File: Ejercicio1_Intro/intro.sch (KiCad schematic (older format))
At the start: 5 parts, among them K1 CONN_3

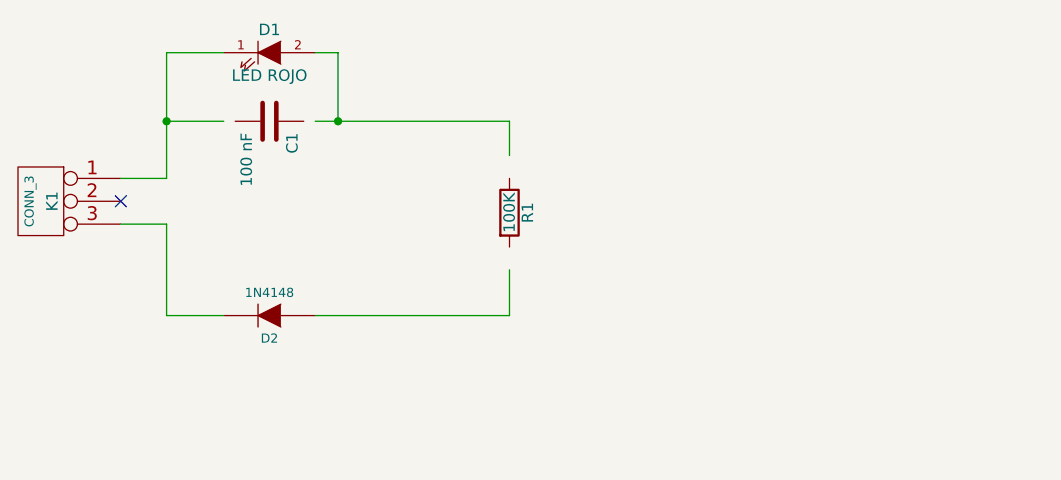
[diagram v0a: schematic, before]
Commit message: Agregado de asociación de footprints en el esquemático.
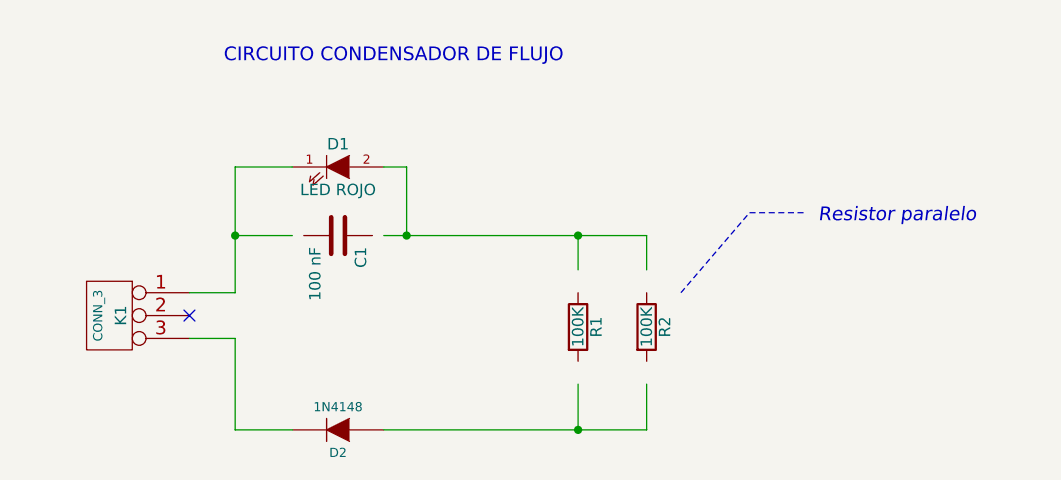
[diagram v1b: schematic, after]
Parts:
- added R2: 100K, footprints_ej1:R3-LARGE_PADS, symbol R
- C1: footprint (none) -> footprints_ej1:C_Rect_L7_W3.5_P5
- D1: footprint (none) -> footprints_ej1:LED-3MM
- D2: footprint (none) -> footprints_ej1:Diode_DO-35_SOD27_Horizontal_RM10
- K1: footprint (none) -> footprints_ej1:bornier3
- R1: footprint (none) -> footprints_ej1:R3-LARGE_PADS
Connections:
- wire segments 13 -> 15
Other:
- note added: "CIRCUITO CONDENSADOR DE FLUJO"
- note added: "Resistor paralelo"
- moved on the sheet: C1, D1, D2, K1, R1
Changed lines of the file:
@@
 LIBS:contrib
 LIBS:valves
+LIBS:intro-cache
 EELAYER 25 0
 EELAYER END
@@
 L C C1
 U 1 1 5638F4A6
-P 5050 3350
-F 0 "C1" H 5100 3450 50  0000 L CNN
-F 1 "100 nF" H 5100 3250 50  0000 L CNN
-F 2 "" H 5050 3350 60  0000 C CNN
-F 3 "" H 5050 3350 60  0000 C CNN
-	1    5050 3350
+P 5350 3850
+F 0 "C1" H 5400 3950 50  0000 L CNN
+F 1 "100 nF" H 5400 3750 50  0000 L CNN
+F 2 "footprints_ej1:C_Rect_L7_W3.5_P5" H 5350 3850 60  0001 C CNN
+F 3 "" H 5350 3850 60  0000 C CNN
+	1    5350 3850
 	0    1    1    0
 $EndComp
@@
 L R R1
 U 1 1 5638F4E1
-P 6100 3750
-F 0 "R1" V 6180 3750 50  0000 C CNN
-F 1 "100K" V 6100 3750 50  0000 C CNN
-F 2 "" H 6100 3750 60  0000 C CNN
-F 3 "" H 6100 3750 60  0000 C CNN
-	1    6100 3750
+P 6400 4250
+F 0 "R1" V 6480 4250 50  0000 C CNN
+F 1 "100K" V 6400 4250 50  0000 C CNN
+F 2 "footprints_ej1:R3-LARGE_PADS" H 6400 4250 60  0001 C CNN
+F 3 "" H 6400 4250 60  0000 C CNN
+	1    6400 4250
 	1    0    0    -1
 $EndComp
@@
 L DIODE D2
 U 1 1 5638F55C
-P 5050 4200
-F 0 "D2" H 5050 4300 40  0000 C CNN
-F 1 "1N4148" H 5050 4100 40  0000 C CNN
-F 2 "" H 5050 4200 60  0000 C CNN
-F 3 "" H 5050 4200 60  0000 C CNN
-	1    5050 4200
+P 5350 4700
+F 0 "D2" H 5350 4800 40  0000 C CNN
+F 1 "1N4148" H 5350 4600 40  0000 C CNN
+F 2 "footprints_ej1:Diode_DO-35_SOD27_Horizontal_RM10" H 5350 4700 60  0001 C CNN
+F 3 "" H 5350 4700 60  0000 C CNN
+	1    5350 4700
 	-1   0    0    1
 $EndComp
 Wire Wire Line
-	4600 3600 4400 3600
+	4900 4100 4700 4100
 Wire Wire Line
-	4600 3050 4600 3600
+	4900 3550 4900 4100
 Wire Wire Line
-	4600 3350 4850 3350
+	4900 3850 5150 3850
 Wire Wire Line
-	5250 3350 6100 3350
+	5550 3850 6700 3850
 Wire Wire Line
-	6100 3350 6100 3500
+	6400 3850 6400 4000
 Wire Wire Line
-	6100 4000 6100 4200
+	6400 4500 6400 4700
 Wire Wire Line
-	6100 4200 5250 4200
+	5550 4700 6700 4700
 Wire Wire Line
-	4850 4200 4600 4200
+	5150 4700 4900 4700
 Wire Wire Line
-	4600 4200 4600 3800
+	4900 4700 4900 4300
 Wire Wire Line
-	4600 3800 4400 3800
+	4900 4300 4700 4300
 $Comp
 L LED D1
 U 1 1 5638F7A0
-P 5050 3050
-F 0 "D1" H 5050 3150 50  0000 C CNN
-F 1 "LED ROJO" H 5050 2950 50  0000 C CNN
-F 2 "" H 5050 3050 60  0000 C CNN
-F 3 "" H 5050 3050 60  0000 C CNN
-	1    5050 3050
+P 5350 3550
+F 0 "D1" H 5350 3650 50  0000 C CNN
+F 1 "LED ROJO" H 5350 3450 50  0000 C CNN
+F 2 "footprints_ej1:LED-3MM" H 5350 3550 60  0001 C CNN
+F 3 "" H 5350 3550 60  0000 C CNN
+	1    5350 3550
 	1    0    0    -1
 $EndComp
 Wire Wire Line
-	5250 3050 5350 3050
+	5550 3550 5650 3550
 Wire Wire Line
-	5350 3050 5350 3350
-Connection ~ 5350 3350
+	5650 3550 5650 3850
+Connection ~ 5650 3850
 Wire Wire Line
-	4850 3050 4600 3050
-Connection ~ 4600 3350
+	5150 3550 4900 3550
+Connection ~ 4900 3850
 $Comp
 L CONN_3 K1
 U 1 1 5638F7EF
-P 4050 3700
-F 0 "K1" V 4000 3700 50  0000 C CNN
-F 1 "CONN_3" V 4100 3700 40  0000 C CNN
-F 2 "" H 4050 3700 60  0000 C CNN
-F 3 "" H 4050 3700 60  0000 C CNN
-	1    4050 3700
+P 4350 4200
+F 0 "K1" V 4300 4200 50  0000 C CNN
+F 1 "CONN_3" V 4400 4200 40  0000 C CNN
+F 2 "footprints_ej1:bornier3" H 4350 4200 60  0001 C CNN
+F 3 "" H 4350 4200 60  0000 C CNN
+	1    4350 4200
 	-1   0    0    -1
 $EndComp
-NoConn ~ 4400 3700
+NoConn ~ 4700 4200
+$Comp
+L R R2
+U 1 1 56390399
+P 6700 4250
+F 0 "R2" V 6780 4250 50  0000 C CNN
+F 1 "100K" V 6700 4250 50  0000 C CNN
+F 2 "footprints_ej1:R3-LARGE_PADS" H 7500 4500 60  0001 C CNN
+F 3 "" H 6700 4250 60  0000 C CNN
+	1    6700 4250
+	1    0    0    -1
+$EndComp
+Wire Wire Line
+	6700 3850 6700 4000
+Connection ~ 6400 3850
+Wire Wire Line
+	6700 4700 6700 4500
+Connection ~ 6400 4700
+Text Notes 4850 3100 0    60   ~ 0
+CIRCUITO CONDENSADOR DE FLUJO
+Wire Notes Line
+	6850 4100 7150 3750
+Wire Notes Line
+	7150 3750 7400 3750
+Text Notes 7450 3800 0    60   Italic 0
+Resistor paralelo
 $EndSCHEMATC

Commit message: Emprolijo esquemático.
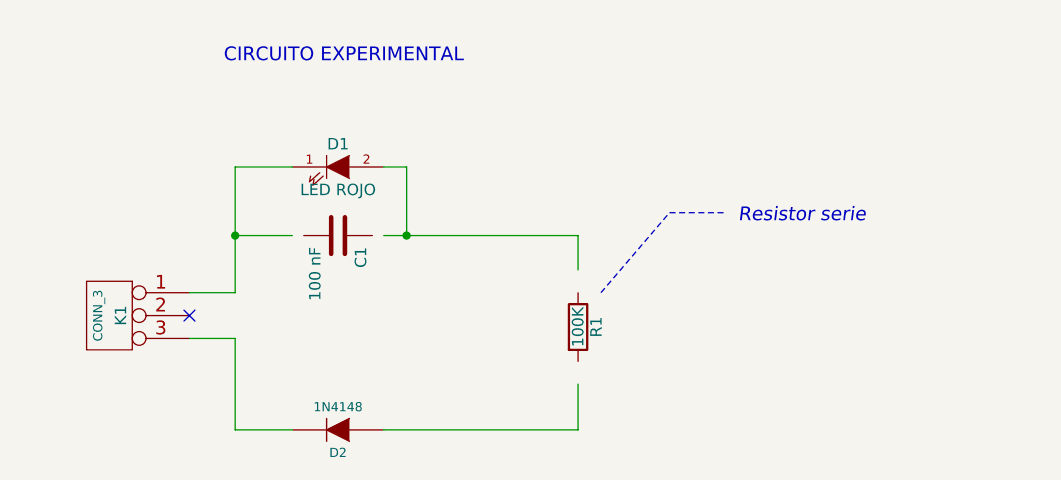
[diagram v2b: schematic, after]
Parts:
- removed R2: 100K, footprints_ej1:R3-LARGE_PADS, symbol R
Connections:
- wire segments 15 -> 13
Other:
- note added: "CIRCUITO EXPERIMENTAL"
- note added: "Resistor serie"
- note removed: "CIRCUITO CONDENSADOR DE FLUJO"
- note removed: "Resistor paralelo"
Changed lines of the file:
@@
 	4900 3850 5150 3850
-Wire Wire Line
-	5550 3850 6700 3850
 Wire Wire Line
 	6400 3850 6400 4000
 Wire Wire Line
 	6400 4500 6400 4700
-Wire Wire Line
-	5550 4700 6700 4700
 Wire Wire Line
 	5150 4700 4900 4700
@@
 $EndComp
 NoConn ~ 4700 4200
-$Comp
-L R R2
-U 1 1 56390399
-P 6700 4250
-F 0 "R2" V 6780 4250 50  0000 C CNN
-F 1 "100K" V 6700 4250 50  0000 C CNN
-F 2 "footprints_ej1:R3-LARGE_PADS" H 7500 4500 60  0001 C CNN
-F 3 "" H 6700 4250 60  0000 C CNN
-	1    6700 4250
-	1    0    0    -1
-$EndComp
+Text Notes 4850 3100 0    60   ~ 0
+CIRCUITO EXPERIMENTAL
+Wire Notes Line
+	6500 4100 6800 3750
+Wire Notes Line
+	6800 3750 7050 3750
+Text Notes 7100 3800 0    60   Italic 0
+Resistor serie
 Wire Wire Line
-	6700 3850 6700 4000
-Connection ~ 6400 3850
+	5550 3850 6400 3850
 Wire Wire Line
-	6700 4700 6700 4500
-Connection ~ 6400 4700
-Text Notes 4850 3100 0    60   ~ 0
-CIRCUITO CONDENSADOR DE FLUJO
-Wire Notes Line
-	6850 4100 7150 3750
-Wire Notes Line
-	7150 3750 7400 3750
-Text Notes 7450 3800 0    60   Italic 0
-Resistor paralelo
+	6400 4700 5550 4700
 $EndSCHEMATC

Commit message: Agregado el PCB y varios archivos intermedios. Tambien .ib y 3ds.
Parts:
- D1: value LED ROJO -> LED ROJO 5mm
- D2: symbol DIODE -> D
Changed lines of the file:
@@
 EESchema Schematic File Version 2
-LIBS:power
 LIBS:device
-LIBS:transistors
 LIBS:conn
-LIBS:linear
-LIBS:regul
-LIBS:74xx
-LIBS:cmos4000
-LIBS:adc-dac
-LIBS:memory
-LIBS:xilinx
-LIBS:special
-LIBS:microcontrollers
-LIBS:dsp
-LIBS:microchip
-LIBS:analog_switches
-LIBS:motorola
-LIBS:texas
-LIBS:intel
-LIBS:audio
-LIBS:interface
-LIBS:digital-audio
-LIBS:philips
-LIBS:display
-LIBS:cypress
-LIBS:siliconi
-LIBS:opto
-LIBS:atmel
-LIBS:contrib
-LIBS:valves
 LIBS:intro-cache
 EELAYER 25 0
@@
 	1    0    0    -1
 $EndComp
-$Comp
-L DIODE D2
-U 1 1 5638F55C
-P 5350 4700
-F 0 "D2" H 5350 4800 40  0000 C CNN
-F 1 "1N4148" H 5350 4600 40  0000 C CNN
-F 2 "footprints_ej1:Diode_DO-35_SOD27_Horizontal_RM10" H 5350 4700 60  0001 C CNN
-F 3 "" H 5350 4700 60  0000 C CNN
-	1    5350 4700
-	-1   0    0    1
-$EndComp
 Wire Wire Line
 	4900 4100 4700 4100
@@
 	4900 3550 4900 4100
 Wire Wire Line
-	4900 3850 5150 3850
+	4900 3850 5200 3850
 Wire Wire Line
-	6400 3850 6400 4000
+	6400 3850 6400 4100
 Wire Wire Line
-	6400 4500 6400 4700
+	6400 4700 6400 4400
 Wire Wire Line
-	5150 4700 4900 4700
+	4900 4700 5200 4700
 Wire Wire Line
 	4900 4700 4900 4300
 Wire Wire Line
 	4900 4300 4700 4300
-$Comp
-L LED D1
-U 1 1 5638F7A0
-P 5350 3550
-F 0 "D1" H 5350 3650 50  0000 C CNN
-F 1 "LED ROJO" H 5350 3450 50  0000 C CNN
-F 2 "footprints_ej1:LED-3MM" H 5350 3550 60  0001 C CNN
-F 3 "" H 5350 3550 60  0000 C CNN
-	1    5350 3550
-	1    0    0    -1
-$EndComp
 Wire Wire Line
 	5550 3550 5650 3550
@@
 Resistor serie
 Wire Wire Line
-	5550 3850 6400 3850
+	5500 3850 6400 3850
 Wire Wire Line
-	6400 4700 5550 4700
+	5500 4700 6400 4700
+$Comp
+L LED D1
+U 1 1 564A13E0
+P 5350 3550
+F 0 "D1" H 5350 3650 50  0000 C CNN
+F 1 "LED ROJO 5mm" H 5350 3400 50  0000 C CNN
+F 2 "footprints_ej1:LED-3MM" H 5350 3550 60  0001 C CNN
+F 3 "" H 5350 3550 60  0000 C CNN
+	1    5350 3550
+	-1   0    0    1
+$EndComp
+$Comp
+L D D2
+U 1 1 5638F55C
+P 5350 4700
+F 0 "D2" H 5350 4800 40  0000 C CNN
+F 1 "1N4148" H 5350 4600 40  0000 C CNN
+F 2 "footprints_ej1:Diode_DO-35_SOD27_Horizontal_RM10" H 5350 4700 60  0001 C CNN
+F 3 "" H 5350 4700 60  0000 C CNN
+	1    5350 4700
+	1    0    0    -1
+$EndComp
 $EndSCHEMATC

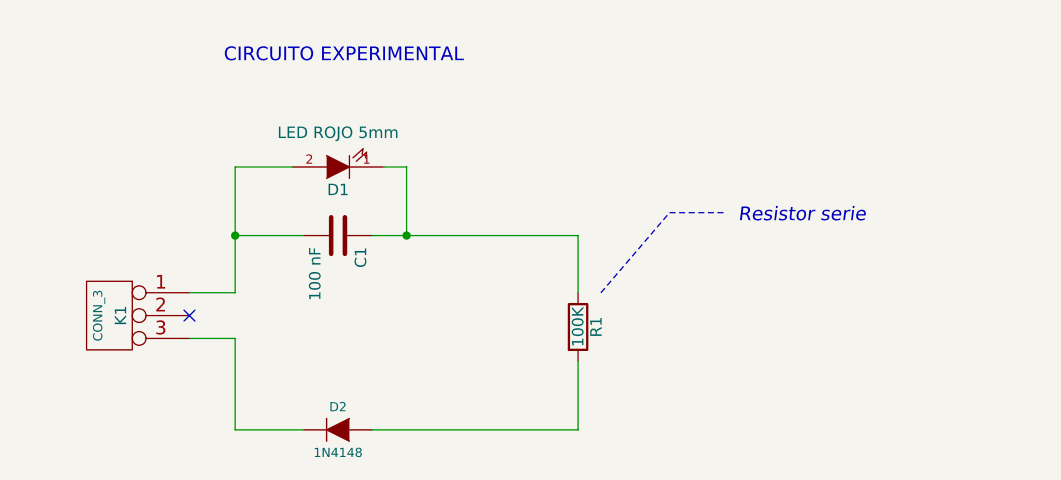
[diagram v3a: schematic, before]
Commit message: Agregado de la R2.
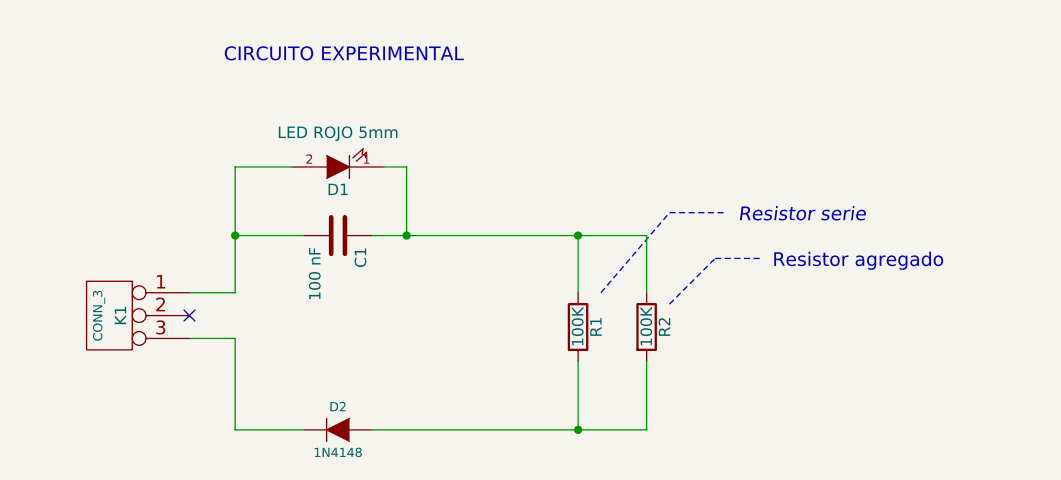
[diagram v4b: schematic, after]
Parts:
- added R2: 100K, footprints_ej1:R3-LARGE_PADS, symbol R
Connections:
- net at C1.1, D1.1 (K), R1.1: now also R2.1
- net at D2.2 (A), R1.2: now also R2.2
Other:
- note added: "Resistor agregado"
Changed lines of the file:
@@
 Resistor serie
 Wire Wire Line
-	5500 3850 6400 3850
+	5500 3850 6700 3850
 Wire Wire Line
-	5500 4700 6400 4700
+	5500 4700 6700 4700
 $Comp
 L LED D1
@@
 	1    0    0    -1
 $EndComp
+$Comp
+L R R2
+U 1 1 564A3B91
+P 6700 4250
+F 0 "R2" V 6780 4250 50  0000 C CNN
+F 1 "100K" V 6700 4250 50  0000 C CNN
+F 2 "footprints_ej1:R3-LARGE_PADS" V 6630 4250 30  0001 C CNN
+F 3 "" H 6700 4250 30  0000 C CNN
+	1    6700 4250
+	1    0    0    -1
+$EndComp
+Wire Wire Line
+	6700 3850 6700 4100
+Connection ~ 6400 3850
+Wire Wire Line
+	6700 4700 6700 4400
+Connection ~ 6400 4700
+Wire Notes Line
+	6800 4150 7000 3950
+Wire Notes Line
+	7000 3950 7200 3950
+Text Notes 7250 4000 0    60   ~ 0
+Resistor agregado
 $EndSCHEMATC
